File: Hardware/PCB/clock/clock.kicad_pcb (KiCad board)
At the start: 2 copper layers, 146 x 170.5 mm, 63 parts, among them J1 AudioJack2, J2 Synth_power_2x5, J3 AudioJack2, J4 AudioJack2, J5 AudioJack2, J6 AudioJack2, J7 AudioJack2, J8 Conn_02x04_Odd_Even, J9 Conn_02x04_Odd_Even, Q1 2N3904, SW1 RotaryEncoder, SW2 SW_Push, U1 40106

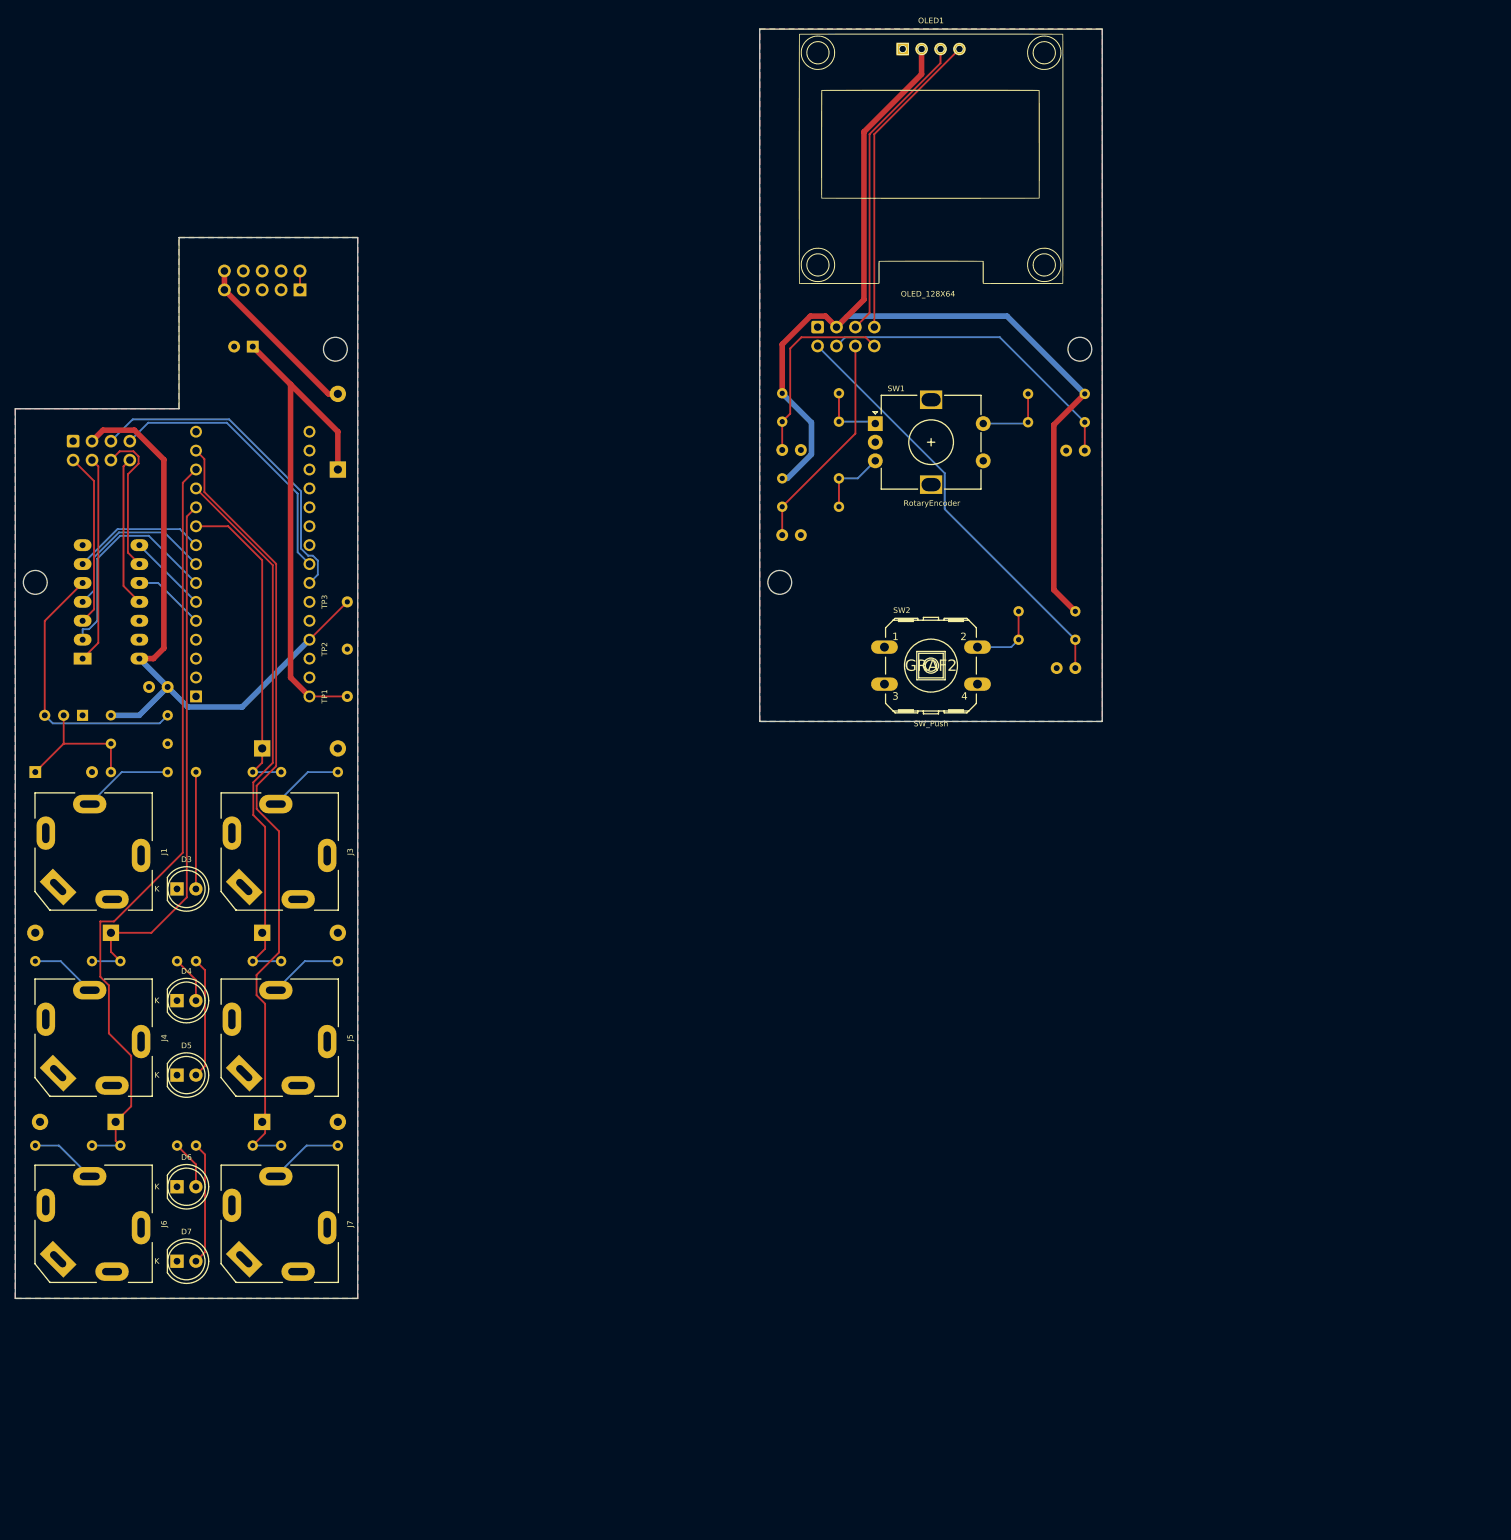
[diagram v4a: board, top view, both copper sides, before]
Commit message: Reset counts when changing division; update schematic and layout with beat output, no ext clock, and unimpeded Nano USB
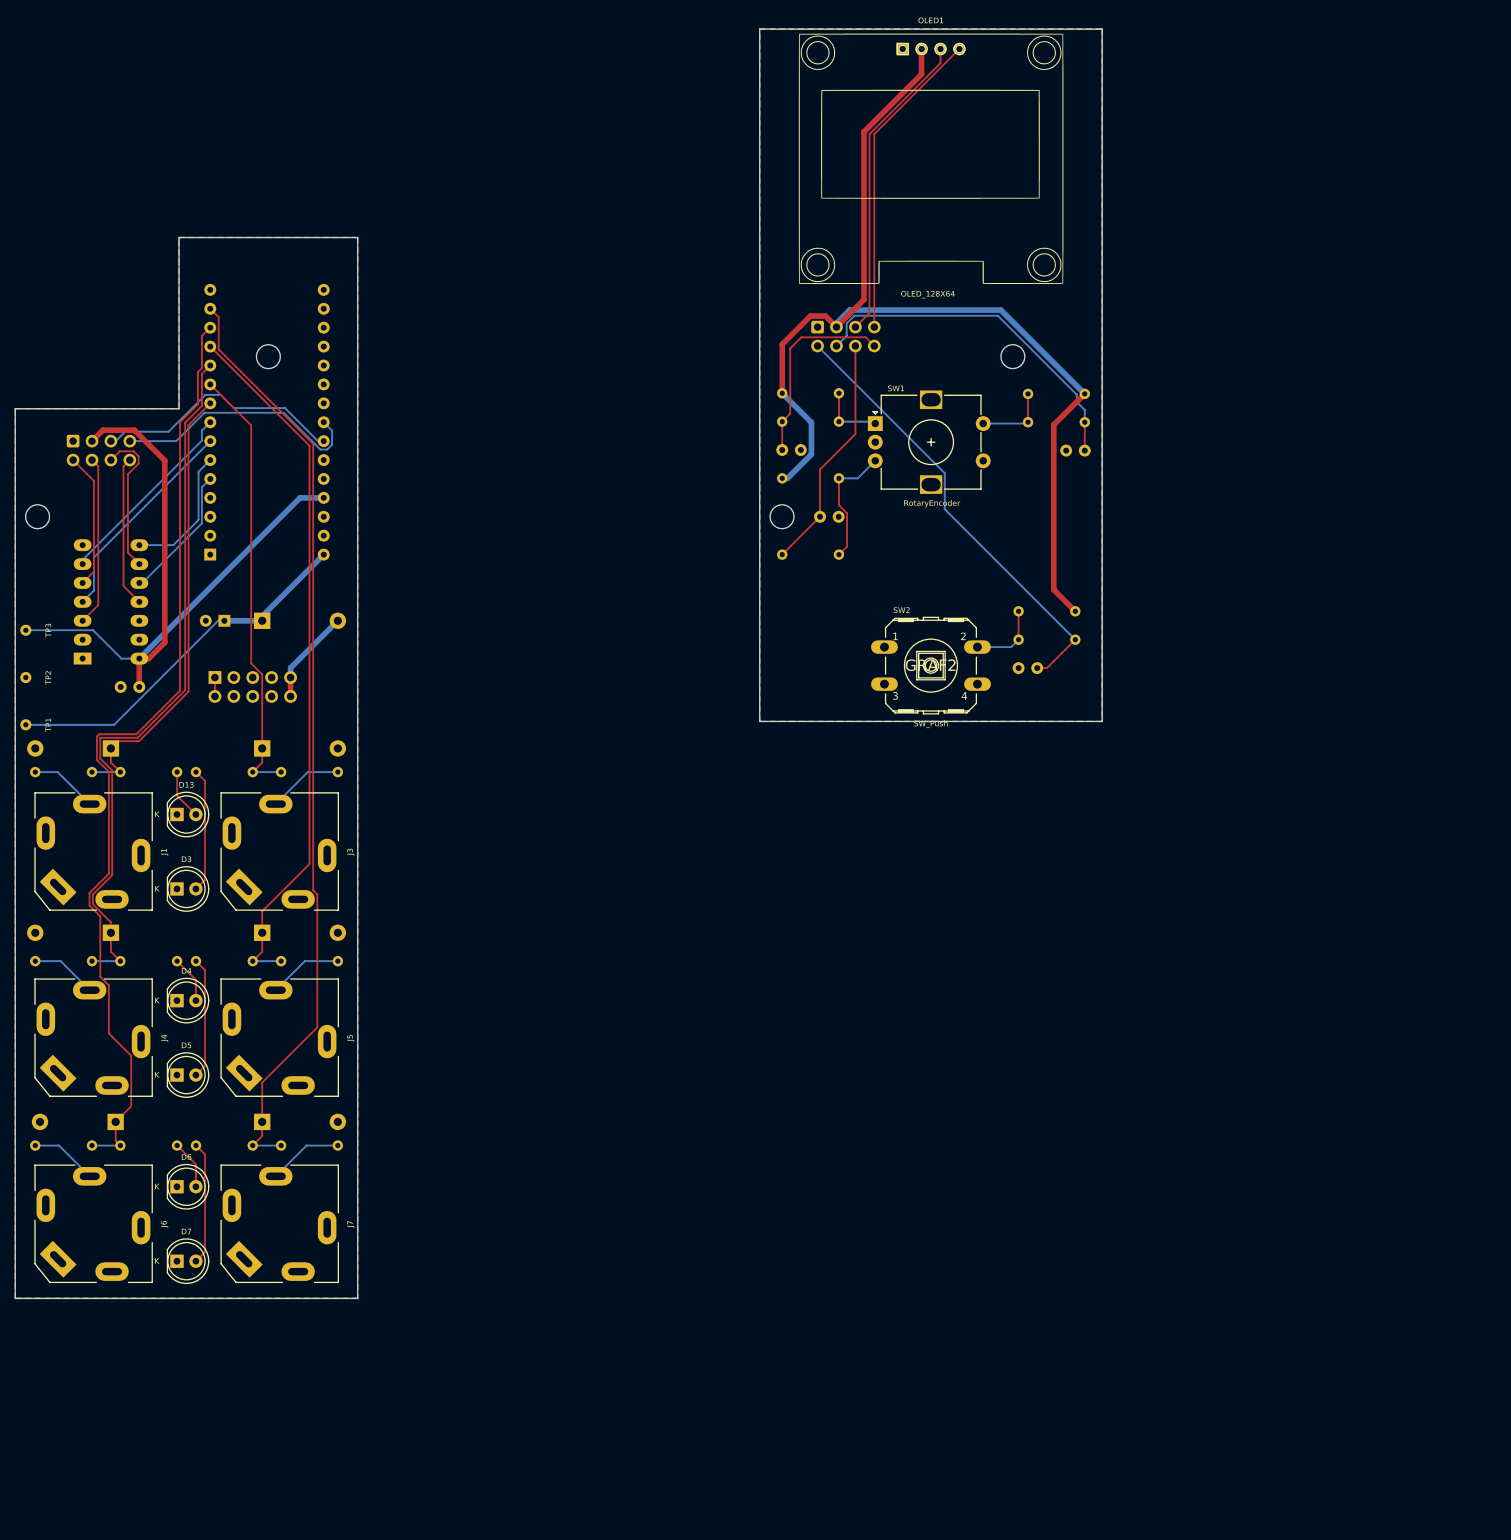
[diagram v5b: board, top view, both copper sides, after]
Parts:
- removed Q1: 2N3904, ao_tht:TO-92_Inline_Wide
- removed R11: 10k, ao_tht:R_Axial_DIN0204_L3.6mm_D1.6mm_P7.62mm_Horizontal
- added D13: LED_red, ao_tht:LED_D5.0mm, F.Cu at (78.7, 120.0)
- A1: footprint Module:Arduino_Nano -> ao_tht:Arduino_Nano
- D1: value 1N4148 -> 1N4733A; footprint ao_tht:D_DO-35_SOD27_P7.62mm_Horizontal -> ao_tht:D_DO-41_SOD81_P10.16mm_Horizontal
- R1: value 100k -> RL
- R6: value 1M -> 1k
- moved J2 53.3 mm to (83.8, 101.6), turned to -90 degrees
- moved TP1 43.3 mm to (58.4, 108.0), turned to 90 degrees
- moved TP2 43.3 mm to (58.4, 101.6), turned to 90 degrees
- moved TP3 43.3 mm to (58.4, 95.2), turned to 90 degrees
- moved C5 37.0 mm to (85.1, 94.0)
- moved D2 22.7 mm to (90.2, 94.0), turned to 0 degrees
- moved A1 19.1 mm to (83.2, 85.1)
- moved D1 10.6 mm to (69.8, 111.1), turned to 180 degrees
- moved H1 9.06 mm to (191.0, 58.5)
- moved H2 9.06 mm to (91.0, 58.5)
- moved R1 8.89 mm to (78.7, 114.3), turned to 180 degrees
- moved H3 8.83 mm to (160.0, 80.0)
- moved H4 8.83 mm to (60.0, 80.0)
- moved R8 6.43 mm to (167.6, 85.1)
- moved C2 5.64 mm to (165.1, 80.0)
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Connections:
- net /CLK_OUT_J renamed /CLK_J
- net /CLK_OUT_L renamed /CLK_L
- net /CLOCK_OUT renamed /CLOCK
- A1 pad 9: /CLOCK_IN -> /BEAT
- D1 pad 1: Net-(D1-Pad1) -> /BEAT
- J1 pad T: /CLK_IN_J -> /BEAT_J
- R1 pad 1: Net-(D1-Pad1) -> /BEAT_L
- R1 pad 2: /CLK_IN_J -> /BEAT
- R6 pad 1: Net-(D1-Pad1) -> /BEAT
- R6 pad 2: GND -> /BEAT_J
- U1 pad 1: /ENC_PUSH_JB -> GND
- U1 pad 2: /ENC_PUSH -> unconnected-(U1-Pad2)
- U1 pad 3: /TACT_JB -> /ENC_PUSH_JB
- U1 pad 4: /TACT -> /ENC_PUSH
- U1 pad 5: Net-(Q1-Pad3) -> /TACT_JB
- U1 pad 6: /CLOCK_IN -> /TACT
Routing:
- net /BEAT: track 0.00 -> 59.7 mm
- net Net-(Q1-Pad3): track 37.3 -> 0.00 mm
- net /DIV_8: track 103.9 -> 128.1 mm
- net /DIV_2: track 73.2 -> 96.1 mm
- net /DIV_4: track 74.0 -> 95.0 mm
- net +12V: track 69.3 -> 49.9 mm
- net /DIV_N: track 106.4 -> 125.8 mm
- net Net-(D1-Pad1): track 19.4 -> 0.00 mm
- net /CLOCK_IN: track 18.1 -> 0.00 mm
- net /CLOCK: track 43.6 -> 59.3 mm
- net /CLK_IN_J: track 12.3 -> 0.00 mm
- net /SCL: track 44.8 -> 33.7 mm
- net /+12_IN: track 23.6 -> 12.8 mm
- net /BEAT_J: track 0.00 -> 9.09 mm
- net /ENC_A: track 9.72 -> 18.1 mm
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
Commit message: PCB adjustments
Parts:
- moved TP1 6.35 mm to (58.4, 101.6)
- moved TP2 6.35 mm to (58.4, 95.2)
- moved TP3 6.35 mm to (58.4, 88.9)
- moved D11 0.64 mm to (69.8, 161.3)
- moved R12 0.64 mm to (81.9, 114.3)
- moved R14 0.64 mm to (81.9, 139.7)
- moved R16 0.64 mm to (81.9, 164.5)
- moved R1 0.63 mm to (78.1, 114.3)
- moved R13 0.63 mm to (78.1, 139.7)
- moved R15 0.63 mm to (78.1, 164.5)
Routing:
- net /ENC_B_JB: track 20.2 -> 16.3 mm
- net +12V: track 49.9 -> 46.2 mm
- net +5V: track 95.0 -> 97.1 mm
- net /BEAT: track 59.7 -> 58.8 mm
- net /DIV_4: track 95.0 -> 94.1 mm
- net /DIV_2: track 96.1 -> 95.2 mm
- net /CLOCK: track 59.3 -> 58.4 mm
- net /DIV_N: track 125.8 -> 124.9 mm
- net /SCL: track 33.7 -> 33.1 mm
- net /TACT: track 26.2 -> 25.6 mm
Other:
- outline, holes or cut-outs redrawn

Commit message: PCB touch ups, panel
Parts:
- added GRAF3: Holes, ao_tht:analogoutput_12mm, B.Cu at (90.8, 82.5)
- GRAF2: value Behind -> Holes; footprint clock:clock_panel_holes -> ao_tht:CC0_logo; moved to B.Cu
- moved GRAF2 120.0 mm to (61.0, 85.1), turned to 180 degrees
- moved C2 1.27 mm to (166.4, 80.0)
- moved R7 1.27 mm to (168.9, 67.2)
- moved R8 1.27 mm to (168.9, 85.1)
- moved C1 1.27 mm to (161.3, 71.0)
- moved R2 1.27 mm to (161.3, 63.4)
- moved R3 1.27 mm to (161.3, 74.8)
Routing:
- net /ENC_A_JA: track 26.5 -> 22.3 mm
- net +5V_1: track 144.6 -> 142.7 mm
- net Net-(R3-Pad2): track 17.0 -> 15.7 mm
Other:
- board text added: "CLOCK Controls board"
- board text added: "CLOCK Rich Holmes 7/2022 CC0 1.0"
- board text added: "Main board"
- board text added: "https://github.com/holmesrichards/clock"

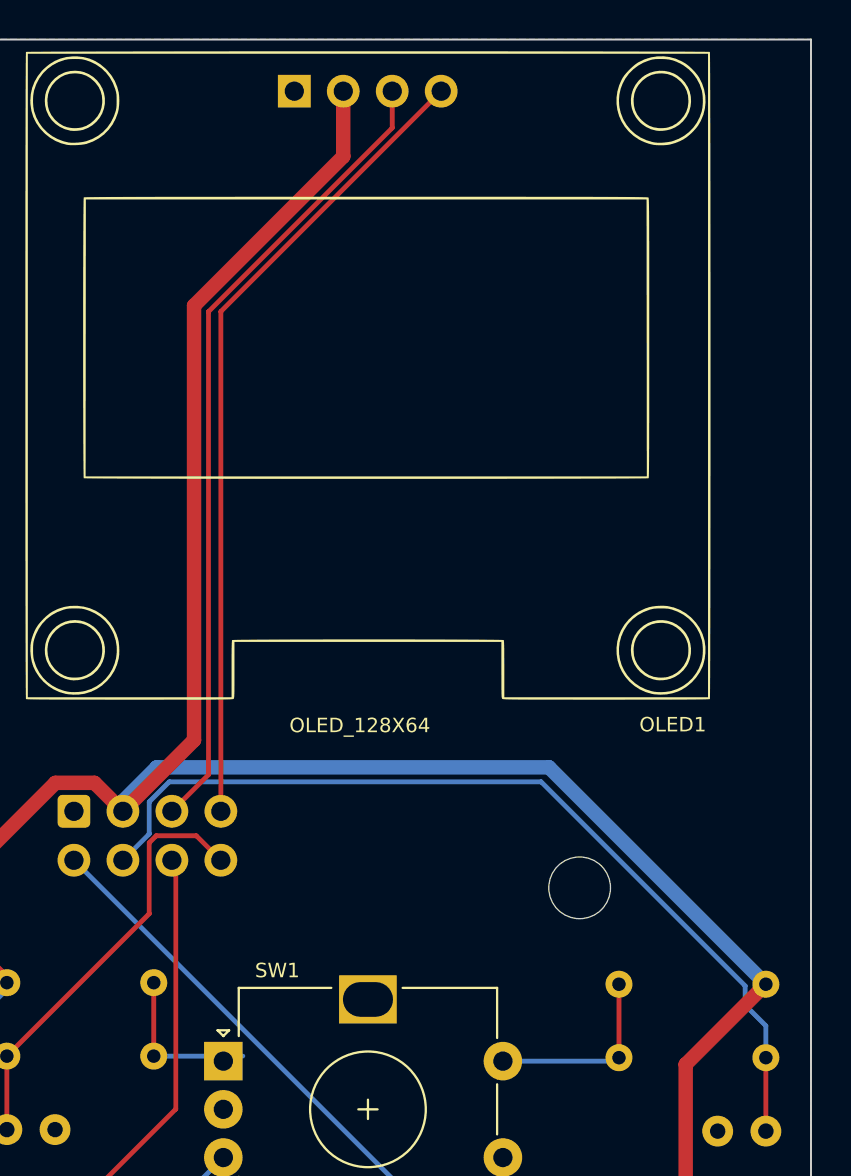
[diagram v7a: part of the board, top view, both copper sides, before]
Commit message: Jumpers for OLED power
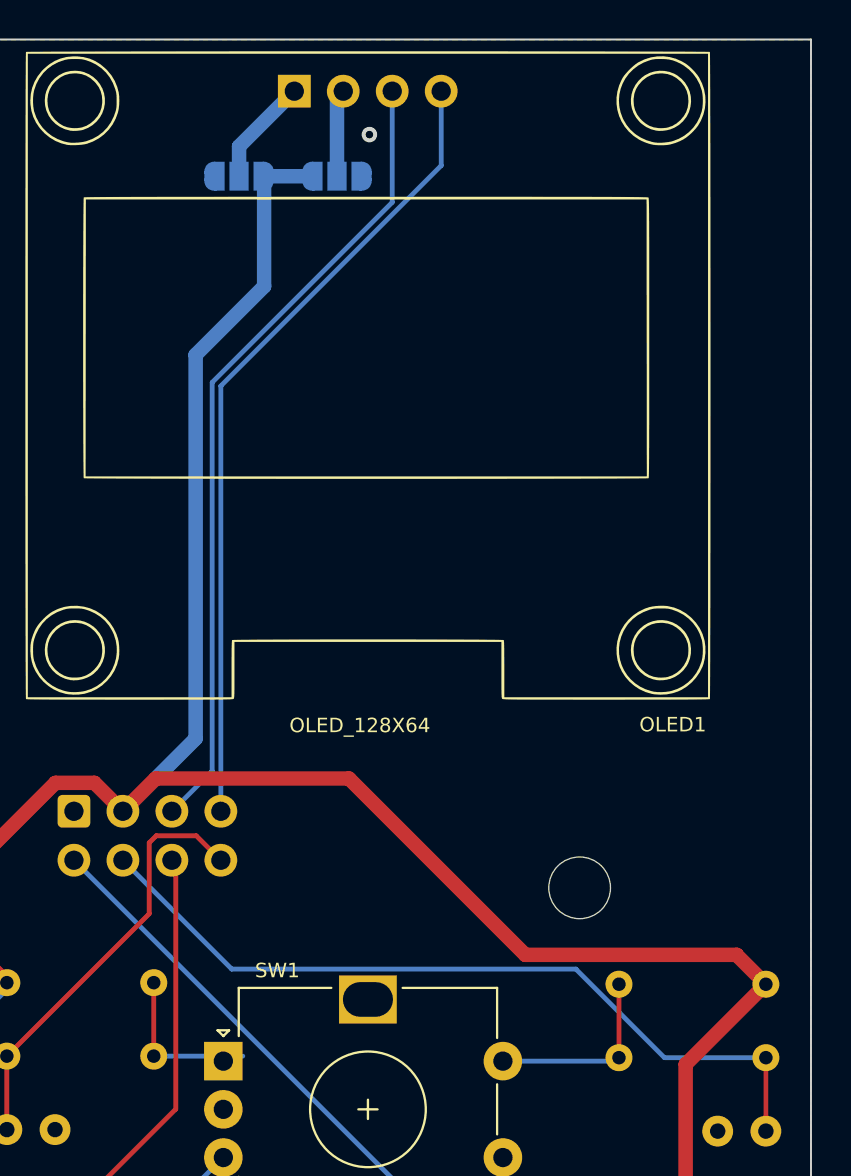
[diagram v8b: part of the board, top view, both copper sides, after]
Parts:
- added JP1: SolderJumper_3_Open, Jumper:SolderJumper-3_P1.3mm_Open_RoundedPad1.0x1.5mm, B.Cu at (173.3, 21.6)
- added JP2: SolderJumper_3_Open, Jumper:SolderJumper-3_P1.3mm_Open_RoundedPad1.0x1.5mm, B.Cu at (178.4, 21.6)
- GRAF2: value Holes -> CC0 logo
- GRAF3: value Holes -> AO logo
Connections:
- net /SCA renamed /SDA
- net /SCA_JA renamed /SDA_JA
- OLED1 pad 1: GND1 -> Net-(OLED1-Pad1)
- OLED1 pad 2: +5V_1 -> Net-(OLED1-Pad2)
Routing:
- net /ENC_PUSH_JA: track 47.3 -> 41.4 mm
- net Net-(OLED1-Pad1): track 0.00 -> 5.60 mm
- net Net-(OLED1-Pad2): track 0.00 -> 4.54 mm
- net +5V_1: track 142.7 -> 138.3 mm
- net GND1: vias 0 -> 1
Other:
- board text added: "Close jumpers as appropriate for OLED power"
- board text added: "GND"
- board text added: "VCC"
